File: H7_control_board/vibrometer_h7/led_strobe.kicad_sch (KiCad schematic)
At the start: 47 parts, among them Q1001 NMOS, Q1002 NMOS, Q1003 NMOS

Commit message: lots of routing progress!!
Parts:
- removed R1001: 22, Resistor_SMD:R_0402_1005Metric, symbol Device:R_Small_US
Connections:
- net LED_STROBE_1: now also Q1001.2 (G), R1002.2, TP1001.1
- net FET2_D: now reaches D1005.1 (K), D1008.1 (K), Q1002.1 (D)
- net FET2_D: now also D1002.1 (K), D1011.1 (K); no longer D1006.1 (K), D1007.1 (K)
- net FET1_D: now reaches D1001.1 (K), D1004.1 (K), Q1001.1 (D)
- net FET1_D: now also D1007.1 (K), D1010.1 (K); no longer D1002.1 (K), D1003.1 (K)
- net FET3_D: now reaches D1009.1 (K), D1012.1 (K), Q1003.1 (D)
- net FET3_D: now also D1003.1 (K), D1006.1 (K); no longer D1010.1 (K), D1011.1 (K)
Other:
- note removed: "LEDs: C210311 C210310 C540978"
- moved on the sheet: C1001, C1002, C1003, C1004, C1005, C1006, C1007, C1008, C1009, C1010, C1011, C1012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

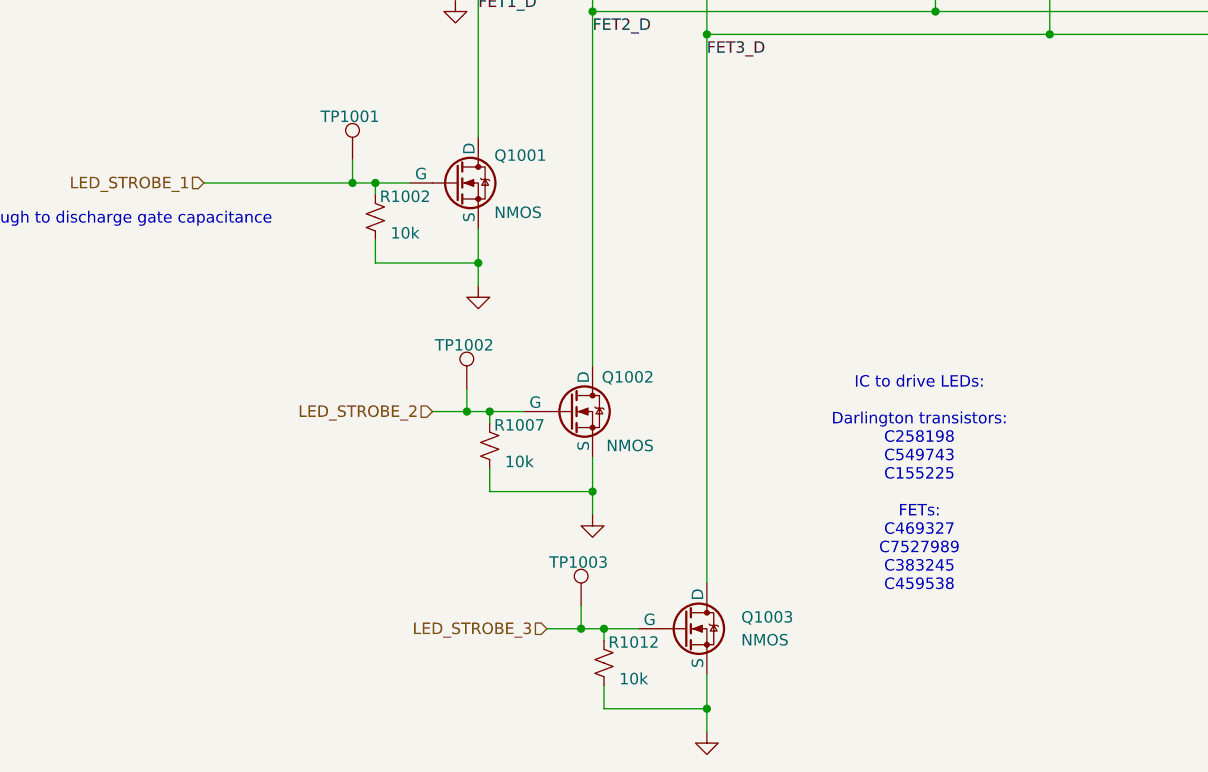
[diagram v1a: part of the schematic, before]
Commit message: connectors, they are so BIG whyyyy john, whyyy
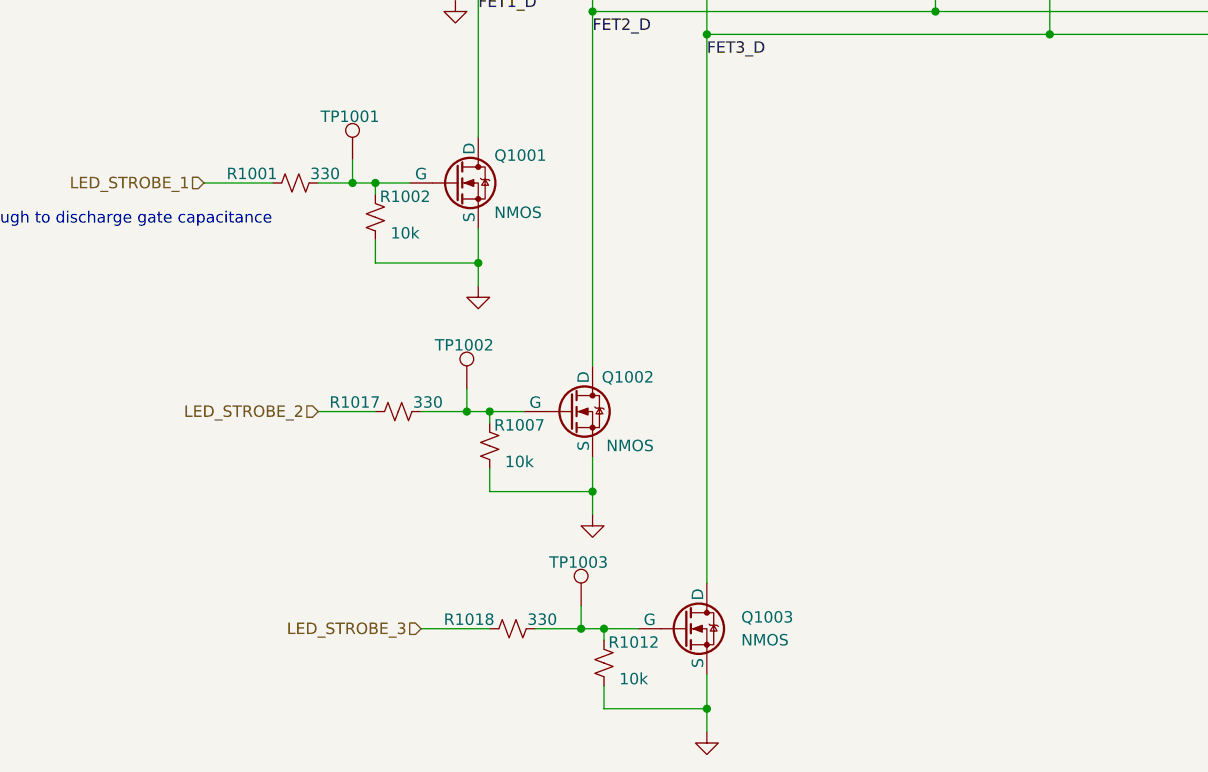
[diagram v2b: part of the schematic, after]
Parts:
- added R1001, R1017, R1018: 330, Resistor_SMD:R_0402_1005Metric, symbol Device:R_Small_US
- Q1001, Q1002, Q1003: footprint (none) -> Package_TO_SOT_SMD:SOT-23; LCSC (none) -> C236116
- R1002, R1007, R1012: footprint Resistor_SMD:R_0603_1608Metric -> Resistor_SMD:R_0402_1005Metric
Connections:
- net LED_STROBE_1: now also R1001.2; no longer Q1001.2 (G), R1002.2, TP1001.1
- net LED_STROBE_2: now also R1017.2; no longer Q1002.2 (G), R1007.2, TP1002.1
- net LED_STROBE_3: now also R1018.2; no longer Q1003.2 (G), R1012.2, TP1003.1
- new net: Q1002.2 (G), R1007.2, R1017.1, TP1002.1
- new net: Q1001.2 (G), R1001.1, R1002.2, TP1001.1
- new net: Q1003.2 (G), R1012.2, R1018.1, TP1003.1
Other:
- note removed: "IC to drive LEDs: Darlington transistors: C258198 C549743 C155225 FETs: C469327 C7527989 C383245 C459538"

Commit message: nearly done....
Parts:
- removed Q1001, Q1002, Q1003: NMOS, Package_TO_SOT_SMD:SOT-23, symbol Simulation_SPICE:NMOS
- added Q1001, Q1002, Q1003: NTR4170N, Package_TO_SOT_SMD:SOT-23, symbol vibrometer_project:NTR4170
- D1001, D1002, D1003, D1004, D1005, D1006, D1007, D1008, D1009, D1010, D1011, D1012: value LED -> LED_WHT
- renumbered R1003 to R1001, R1004 to R1002, R1005 to R1003, R1006 to R1004, R1008 to R1005, R1009 to R1006, R1010 to R1007, R1011 to R1008, R1013 to R1009, R1014 to R1010, R1015 to R1011, R1016 to R1012, R1001 to R1013, R1002 to R1014, R1017 to R1015, R1007 to R1016, R1018 to R1017, R1012 to R1018
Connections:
- net FET1_D: now also Q1001.3 (D)
- net FET2_D: now also Q1002.3 (D)
- net FET3_D: now also Q1003.3 (D)
- net GND: now also Q1001.2 (S), Q1002.2 (S), Q1003.2 (S)
- net at R1015.1, R1016.2, TP1002.1: now also Q1002.1 (G)
- net at R1013.1, R1014.2, TP1001.1: now also Q1001.1 (G)
- net at R1017.1, R1018.2, TP1003.1: now also Q1003.1 (G)
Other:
- note removed: "check if this value is enough to discharge gate capacitance"

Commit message: checked all footprints, made tiny daughterboard
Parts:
- R1001, R1002, R1003, R1004, R1005, R1006, R1007, R1008, R1009, R1010, R1011, R1012: value ?? -> 30; LCSC (none) -> C5552472
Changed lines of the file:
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@@
 			)
 		)
-		(property "Value" "??"
+		(property "Value" "30"
 			(at 240.792 65.278 0)
 			(effects
@@
 			)
 		)
-		(property "Datasheet" "~"
+		(property "Datasheet" "https://www.lcsc.com/datasheet/lcsc_datasheet_2404151502_YAGEO-AC0805FR-7W30RL_C5552472.pdf"
 			(at 237.49 63.5 0)
 			(effects
@@
 			)
 		)
-		(property "LCSC" ""
+		(property "LCSC" "C5552472 "
 			(at 237.49 63.5 0)
 			(effects
@@
 			)
 		)
-		(property "Value" "??"
+		(property "Value" "30"
 			(at 113.792 65.278 0)
 			(effects
@@
 			)
 		)
-		(property "Datasheet" "~"
+		(property "Datasheet" "https://www.lcsc.com/datasheet/lcsc_datasheet_2404151502_YAGEO-AC0805FR-7W30RL_C5552472.pdf"
 			(at 110.49 63.5 0)
 			(effects
@@
 			)
 		)
-		(property "LCSC" ""
+		(property "LCSC" "C5552472 "
 			(at 110.49 63.5 0)
 			(effects
@@
 			)
 		)
-		(property "Value" "??"
+		(property "Value" "30"
 			(at 215.392 65.278 0)
 			(effects
@@
 			)
 		)
-		(property "Datasheet" "~"
+		(property "Datasheet" "https://www.lcsc.com/datasheet/lcsc_datasheet_2404151502_YAGEO-AC0805FR-7W30RL_C5552472.pdf"
 			(at 212.09 63.5 0)
 			(effects
@@
 			)
 		)
-		(property "LCSC" ""
+		(property "LCSC" "C5552472 "
 			(at 212.09 63.5 0)
 			(effects
@@
 			)
 		)
-		(property "Value" "??"
+		(property "Value" "30"
 			(at 189.992 65.278 0)
 			(effects
@@
 			)
 		)
-		(property "Datasheet" "~"
+		(property "Datasheet" "https://www.lcsc.com/datasheet/lcsc_datasheet_2404151502_YAGEO-AC0805FR-7W30RL_C5552472.pdf"
 			(at 186.69 63.5 0)
 			(effects
@@
 			)
 		)
-		(property "LCSC" ""
+		(property "LCSC" "C5552472 "
 			(at 186.69 63.5 0)
 			(effects
@@
 			)
 		)
-		(property "Value" "??"
+		(property "Value" "30"
 			(at 126.492 65.278 0)
 			(effects
@@
 			)
 		)
-		(property "Datasheet" "~"
+		(property "Datasheet" "https://www.lcsc.com/datasheet/lcsc_datasheet_2404151502_YAGEO-AC0805FR-7W30RL_C5552472.pdf"
 			(at 123.19 63.5 0)
 			(effects
@@
 			)
 		)
-		(property "LCSC" ""
+		(property "LCSC" "C5552472 "
 			(at 123.19 63.5 0)
 			(effects
@@
 			)
 		)
-		(property "Value" "??"
+		(property "Value" "30"
 			(at 151.892 65.278 0)
 			(effects
@@
 			)
 		)
-		(property "Datasheet" "~"
+		(property "Datasheet" "https://www.lcsc.com/datasheet/lcsc_datasheet_2404151502_YAGEO-AC0805FR-7W30RL_C5552472.pdf"
 			(at 148.59 63.5 0)
 			(effects
@@
 			)
 		)
-		(property "LCSC" ""
+		(property "LCSC" "C5552472 "
 			(at 148.59 63.5 0)
 			(effects
@@
 			)
 		)
-		(property "Value" "??"
+		(property "Value" "30"
 			(at 139.192 65.278 0)
 			(effects
@@
 			)
 		)
-		(property "Datasheet" "~"
+		(property "Datasheet" "https://www.lcsc.com/datasheet/lcsc_datasheet_2404151502_YAGEO-AC0805FR-7W30RL_C5552472.pdf"
 			(at 135.89 63.5 0)
 			(effects
@@
 			)
 		)
-		(property "LCSC" ""
+		(property "LCSC" "C5552472 "
 			(at 135.89 63.5 0)
 			(effects
@@
 			)
 		)
-		(property "Value" "??"
+		(property "Value" "30"
 			(at 101.092 65.278 0)
 			(effects
@@
 			)
 		)
-		(property "Datasheet" "~"
+		(property "Datasheet" "https://www.lcsc.com/datasheet/lcsc_datasheet_2404151502_YAGEO-AC0805FR-7W30RL_C5552472.pdf"
 			(at 97.79 63.5 0)
 			(effects
@@
 			)
 		)
-		(property "LCSC" ""
+		(property "LCSC" "C5552472 "
 			(at 97.79 63.5 0)
 			(effects
@@
 			)
 		)
-		(property "Value" "??"
+		(property "Value" "30"
 			(at 228.092 65.278 0)
 			(effects
@@
 			)
 		)
-		(property "Datasheet" "~"
+		(property "Datasheet" "https://www.lcsc.com/datasheet/lcsc_datasheet_2404151502_YAGEO-AC0805FR-7W30RL_C5552472.pdf"
 			(at 224.79 63.5 0)
 			(effects
@@
 			)
 		)
-		(property "LCSC" ""
+		(property "LCSC" "C5552472 "
 			(at 224.79 63.5 0)
 			(effects
@@
 			)
 		)
-		(property "Value" "??"
+		(property "Value" "30"
 			(at 177.292 65.278 0)
 			(effects
@@
 			)
 		)
-		(property "Datasheet" "~"
+		(property "Datasheet" "https://www.lcsc.com/datasheet/lcsc_datasheet_2404151502_YAGEO-AC0805FR-7W30RL_C5552472.pdf"
 			(at 173.99 63.5 0)
 			(effects
@@
 			)
 		)
-		(property "LCSC" ""
+		(property "LCSC" "C5552472 "
 			(at 173.99 63.5 0)
 			(effects
@@
 			)
 		)
-		(property "Value" "??"
+		(property "Value" "30"
 			(at 202.692 65.278 0)
 			(effects
@@
 			)
 		)
-		(property "Datasheet" "~"
+		(property "Datasheet" "https://www.lcsc.com/datasheet/lcsc_datasheet_2404151502_YAGEO-AC0805FR-7W30RL_C5552472.pdf"
 			(at 199.39 63.5 0)
 			(effects
@@
 			)
 		)
-		(property "LCSC" ""
+		(property "LCSC" "C5552472 "
 			(at 199.39 63.5 0)
 			(effects
@@
 			)
 		)
-		(property "Value" "??"
+		(property "Value" "30"
 			(at 164.592 65.278 0)
 			(effects
@@
 			)
 		)
-		(property "Datasheet" "~"
+		(property "Datasheet" "https://www.lcsc.com/datasheet/lcsc_datasheet_2404151502_YAGEO-AC0805FR-7W30RL_C5552472.pdf"
 			(at 161.29 63.5 0)
 			(effects
@@
 			)
 		)
-		(property "LCSC" ""
+		(property "LCSC" "C5552472 "
 			(at 161.29 63.5 0)
 			(effects
